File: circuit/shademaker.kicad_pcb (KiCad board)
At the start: 2 copper layers, 67.9 x 43.8 mm, 15 parts, among them M1 Jumper_NO_Small, M2 Jumper_NO_Small, Q1 IRLZ44N, SW1 I²C ADDRESS

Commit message: Cleanup
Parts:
- SCREW1: footprint TerminalBlock_4Ucon:TerminalBlock_4Ucon_1x09_P3.50mm_Vertical -> TerminalBlock_Phoenix:TerminalBlock_Phoenix_PT-1,5-9-3.5-H_1x09_P3.50mm_Horizontal

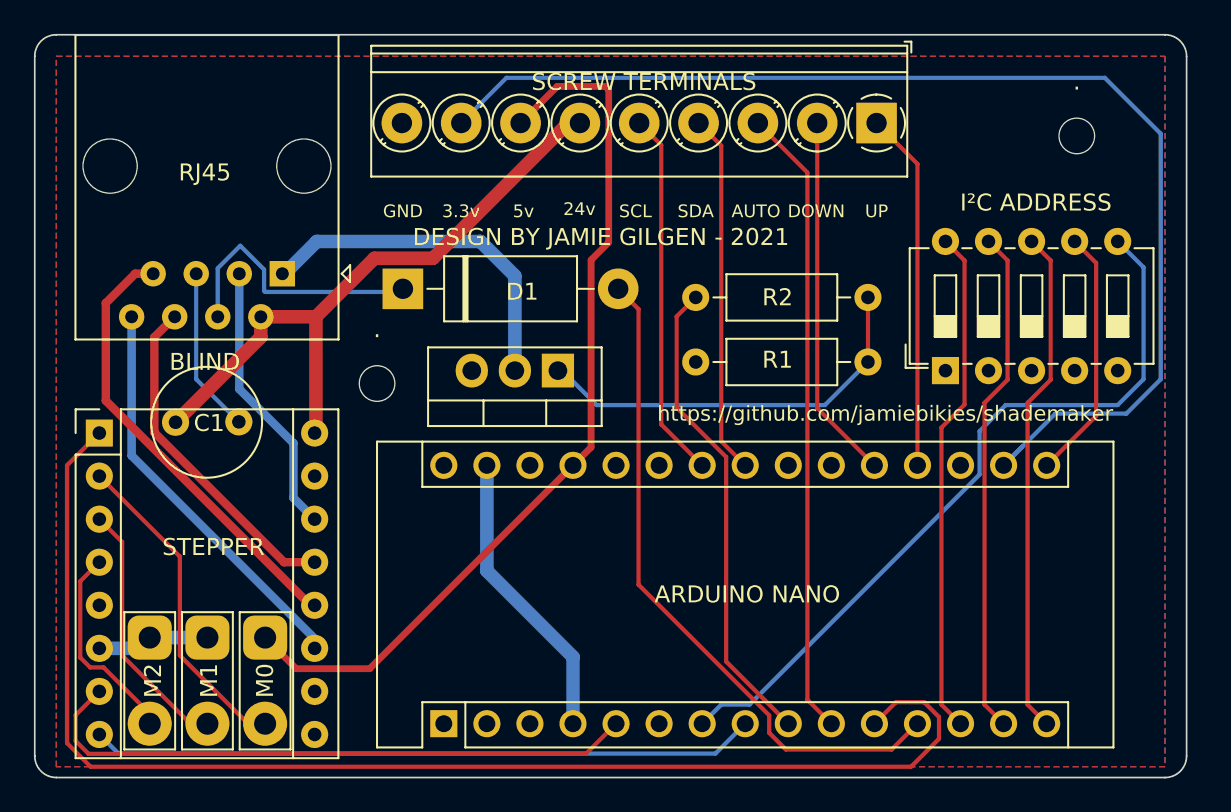
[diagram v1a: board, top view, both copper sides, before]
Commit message: Add platform.io setup to project
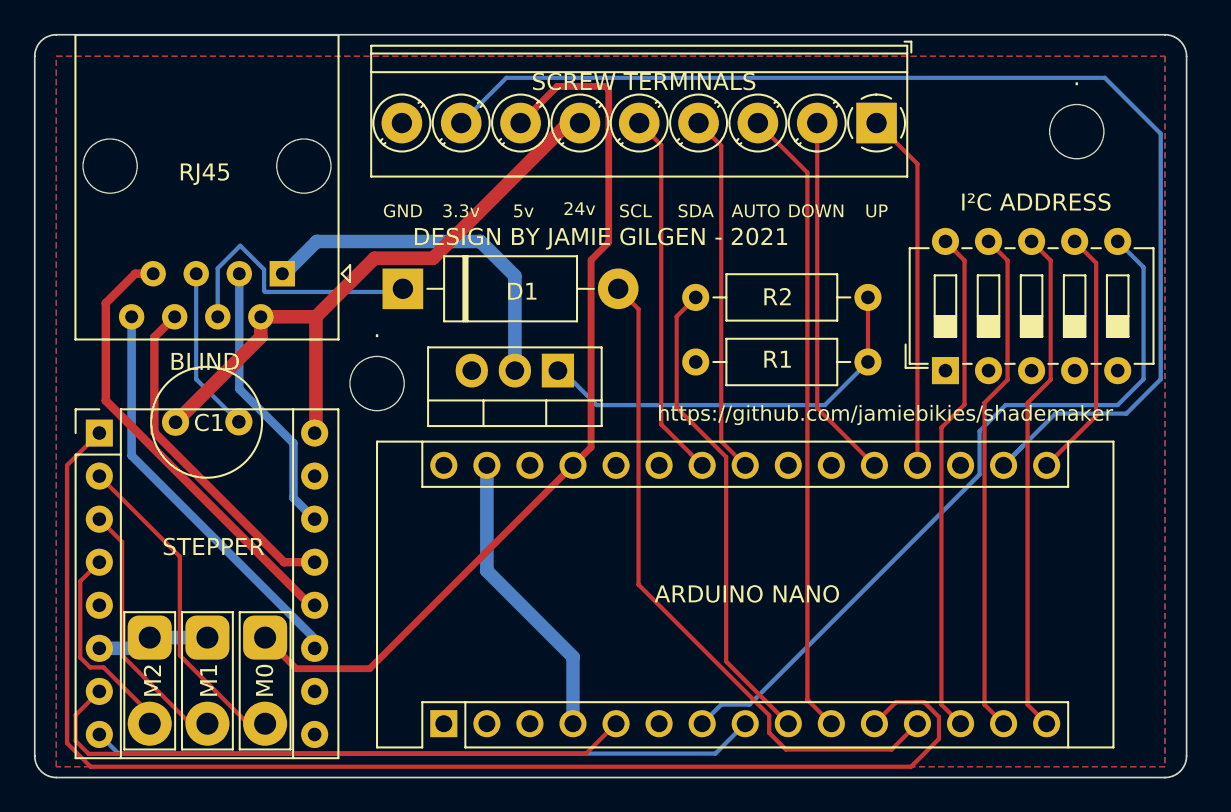
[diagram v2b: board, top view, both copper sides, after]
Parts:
- . (x2): value MountingHole_2.1mm -> MountingHole_3.2mm_M3; footprint MountingHole:MountingHole_2.1mm -> MountingHole:MountingHole_3.2mm_M3
- moved . 0.25 mm to (184.0, 83.2)
